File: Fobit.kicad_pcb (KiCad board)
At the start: 2 copper layers, 25.4 x 44.5 mm, 20 parts, among them J1 Conn_01x02, U1 nRF52840, U2 NPM1100-QDAA-R

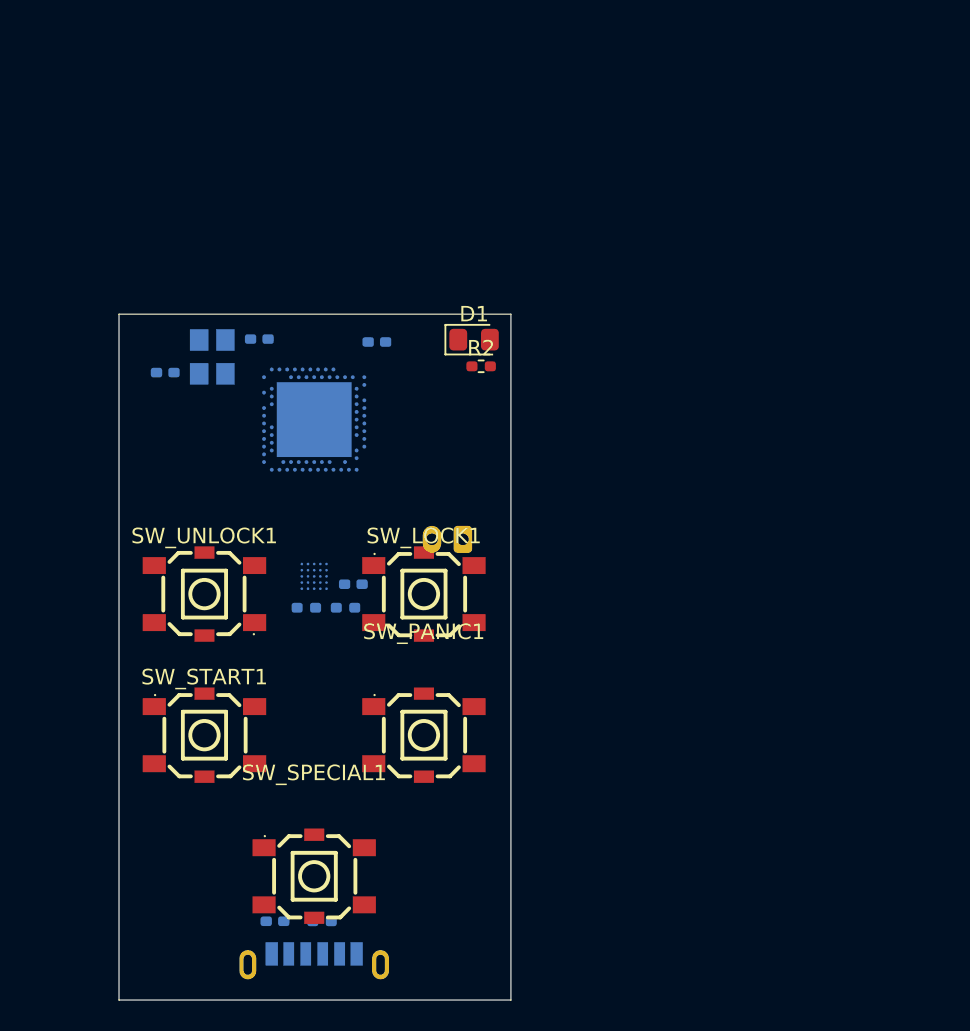
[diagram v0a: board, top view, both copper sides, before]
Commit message: Corrected USB host/slave resistors. Added REG1 DC-DC stage. Removed X2, added X1.
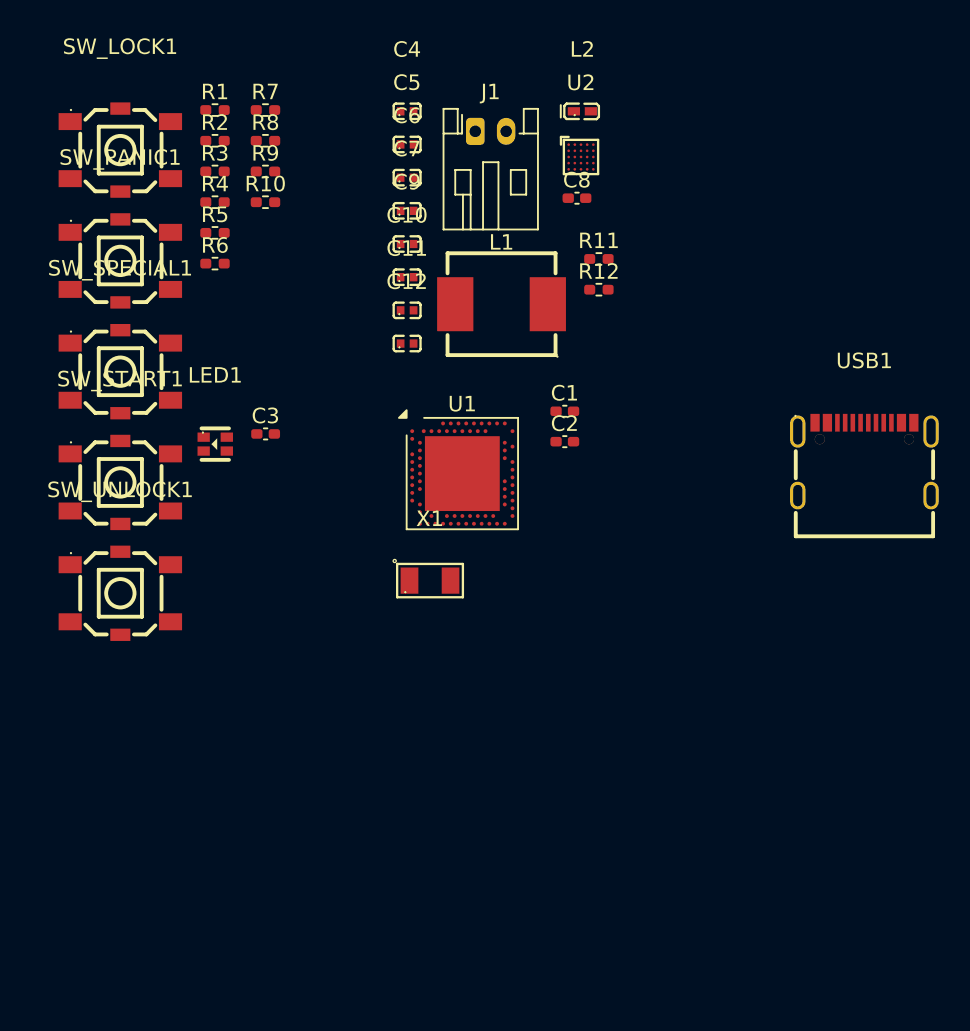
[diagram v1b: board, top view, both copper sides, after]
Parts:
- removed CRYSTAL1: CF4032M00012001, easyeda2kicad:CRYSTAL-SMD_4P-L3.2-W2.5-BL_SIT8008BI
- removed D1: STATUS_LED, LED_SMD:LED_0805_2012Metric_Pad1.15x1.40mm_HandSolder
- added C10: 0402B104K250NT, MyLib:C0402, F.Cu at (158.4, 77.1)
- added C11: TCC0402X5R475M6R3AT, MyLib:C0402, F.Cu at (158.4, 79.3)
- added C12: 0402CG101J500NT, MyLib:C0402, F.Cu at (158.4, 81.4)
- added C4: TCC0402X5R475M6R3AT, MyLib:C0402, F.Cu at (158.4, 66.4)
- added C5: TCC0402X5R475M6R3AT, MyLib:C0402, F.Cu at (158.4, 68.5)
- added C6: CL05A105KA5NQNC, MyLib:C0402, F.Cu at (158.4, 70.7)
- added C9: TCC0402X5R475M6R3AT, MyLib:C0402, F.Cu at (158.4, 75.0)
- added L1: FXL0630-100-M, MyLib:IND-SMD_L7.3-W6.8, F.Cu at (164.5, 78.9)
- added L2: VHF100505HQ15NJT, MyLib:L0402-R-RD, F.Cu at (169.8, 66.4)
- added LED1: SZYY1615RGB-A 4PIN, MyLib:LED-ARRAY-SMD_4P-L1.6-W1.5_SZYY1615RGB-A, F.Cu at (146.0, 87.9)
- added R1: R_Small_US, FobitLib:R_0402_1005Metric_Pad0.72x0.64mm_HandSolder, F.Cu at (146.0, 66.3)
- added R10: R_Small_US, FobitLib:R_0402_1005Metric_Pad0.72x0.64mm_HandSolder, F.Cu at (149.2, 72.3)
- added R11: 4.7kOhms, FobitLib:R_0402_1005Metric_Pad0.72x0.64mm_HandSolder, F.Cu at (170.9, 75.9)
- added R12: 10kOhms, FobitLib:R_0402_1005Metric_Pad0.72x0.64mm_HandSolder, F.Cu at (170.9, 77.9)
- added R3: R_Small_US, FobitLib:R_0402_1005Metric_Pad0.72x0.64mm_HandSolder, F.Cu at (146.0, 70.3)
- added R4: 5.1kOhms, FobitLib:R_0402_1005Metric_Pad0.72x0.64mm_HandSolder, F.Cu at (146.0, 72.3)
- added R5: 5.1kOhms, FobitLib:R_0402_1005Metric_Pad0.72x0.64mm_HandSolder, F.Cu at (146.0, 74.3)
- added R6: R_Small_US, FobitLib:R_0402_1005Metric_Pad0.72x0.64mm_HandSolder, F.Cu at (146.0, 76.2)
- added X1: S3132768092070, MyLib:OSC-SMD_2P-L3.2-W1.5, F.Cu at (159.9, 96.8)
- C1: value 100nF -> 12pF; footprint Capacitor_SMD:C_0402_1005Metric_Pad0.74x0.62mm_HandSolder -> FobitLib:C_0402_1005Metric_Pad0.74x0.62mm_HandSolder; moved to F.Cu
- C2, C8: footprint Capacitor_SMD:C_0402_1005Metric_Pad0.74x0.62mm_HandSolder -> FobitLib:C_0402_1005Metric_Pad0.74x0.62mm_HandSolder; moved to F.Cu
- C3: value 12pF -> 2.2uF; footprint Capacitor_SMD:C_0402_1005Metric_Pad0.74x0.62mm_HandSolder -> FobitLib:C_0402_1005Metric_Pad0.74x0.62mm_HandSolder; moved to F.Cu
- C7: value 2.2uF -> 0402B473K500NT; footprint Capacitor_SMD:C_0402_1005Metric_Pad0.74x0.62mm_HandSolder -> MyLib:C0402; moved to F.Cu
- J1: footprint Connector_JST:JST_PH_S2B-PH-K_1x02_P2.00mm_Horizontal -> FobitLib:JST_PH_S2B-PH-K_1x02_P2.00mm_Horizontal; moved to F.Cu
- R2: value 100Ohms -> R_Small_US; footprint Resistor_SMD:R_0402_1005Metric_Pad0.72x0.64mm_HandSolder -> FobitLib:R_0402_1005Metric_Pad0.72x0.64mm_HandSolder
- R7: value 4.7kOhms -> R_Small_US; footprint Resistor_SMD:R_0402_1005Metric_Pad0.72x0.64mm_HandSolder -> FobitLib:R_0402_1005Metric_Pad0.72x0.64mm_HandSolder; moved to F.Cu
- R8: value 10kOhms -> R_Small_US; footprint Resistor_SMD:R_0402_1005Metric_Pad0.72x0.64mm_HandSolder -> FobitLib:R_0402_1005Metric_Pad0.72x0.64mm_HandSolder; moved to F.Cu
- R9: value 56kOhms -> R_Small_US; footprint Resistor_SMD:R_0402_1005Metric_Pad0.72x0.64mm_HandSolder -> FobitLib:R_0402_1005Metric_Pad0.72x0.64mm_HandSolder; moved to F.Cu
- SW_LOCK1, SW_PANIC1, SW_SPECIAL1, SW_START1, SW_UNLOCK1: footprint easyeda2kicad:SW-SMD_4P-L5.2-W5.2-P3.70-LS6.4_UK-B0233XX -> FobitLib:SW-SMD_4P-L5.2-W5.2-P3.70-LS6.4_UK-B0233XX
- U1: footprint Package_DFN_QFN:Nordic_AQFN-73-1EP_7x7mm_P0.5mm -> FobitLib:Nordic_AQFN-73-1EP_7x7mm_P0.5mm; moved to F.Cu
- U2: footprint easyeda2kicad:WLCSP-25_L2.1-W2.1-R5-C5-P0.40-TL-1 -> FobitLib:WLCSP-25_L2.1-W2.1-R5-C5-P0.40-TL-1; moved to F.Cu
- USB1: value HX TYPE-C 6P LT H5.0 -> TYPE-C16PIN; footprint easyeda2kicad:USB-C-SMD_HX-TYPE-C-6P-LT-H5.0 -> MyLib:USB-C-SMD_TYPE-C16PIN; moved to F.Cu
- moved R9 48.7 mm to (149.2, 70.3), turned to 0 degrees
- moved USB1 48.2 mm to (188.1, 88.9), turned to 0 degrees
- moved C7 46.8 mm to (158.4, 72.8), turned to 0 degrees
- moved SW_PANIC1 36.5 mm to (139.8, 76.1)
- moved SW_SPECIAL1 35.0 mm to (139.8, 83.3)
- moved SW_LOCK1 34.9 mm to (139.8, 68.9)
- moved R7 32.4 mm to (149.2, 66.3)
- moved U2 32.2 mm to (169.7, 69.3), turned to 0 degrees
- moved R8 30.7 mm to (149.2, 68.3)
- moved C8 28.9 mm to (169.4, 72.0)
- moved J1 26.5 mm to (162.8, 67.7), turned to 0 degrees
- moved R2 22.6 mm to (146.0, 68.3)
- moved C2 20.9 mm to (168.6, 87.8)
- moved SW_START1 17.3 mm to (139.8, 90.4)
- moved C1 13.0 mm to (168.6, 85.8)
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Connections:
- C1 pad 1: VBUS -> SOC_XC1
- C3 pad 1: SOC_XC1 -> USBC_V+
- C7 pad 1: USBC_V+ -> SOC_DEC4
- C8 pad 1: VBUS -> SOC_VBUS
- R2 pad 1: STATUS_LED -> LOCK_SIG
- R2 pad 2: Net-(D1-A) -> Net-(R2-Pad2)
- R7 pad 1: BAT_- -> SPECIAL_SIG
- R7 pad 2: Net-(U2-ICHG) -> Net-(R7-Pad2)
- R8 pad 1: Net-(U2-NTC) -> STATUS_LED_R
- R8 pad 2: BAT_- -> Net-(LED1-A-Pad1)
- R9 pad 1: USBC_V+ -> STATUS_LED_G
- R9 pad 2: Net-(USB1-CC1) -> Net-(LED1-A-Pad2)
- SW_LOCK1 pad 1: Net-(R3-Pad2) (its old number) -> Net-(R2-Pad2)
- SW_SPECIAL1 pad 1: Net-(R6-Pad2) (its old number) -> Net-(R7-Pad2)
- U1 pad A22: VBUS -> SOC_VBUS
- U1 pad A23: SOC_XC2 -> unconnected-(U1-XC2-PadA23)
- U1 pad AC17: unconnected-(U1-P0.21-PadAC17) -> UNLOCK_SIG
- U1 pad AC19: unconnected-(U1-P0.23-PadAC19) -> START_SIG
- U1 pad AC21: unconnected-(U1-P0.25-PadAC21) -> SPECIAL_SIG
- U1 pad AC5: unconnected-(U1-DECUSB-PadAC5) -> SOC_DECUSB
- U1 pad AC9: unconnected-(U1-P0.14-PadAC9) -> STATUS_LED_G
- U1 pad AD10: unconnected-(U1-P0.15-PadAD10) -> STATUS_LED_B
- U1 pad AD14: VBUS -> SOC_VBUS
- U1 pad AD18: unconnected-(U1-P0.22-PadAD18) -> LOCK_SIG
- U1 pad AD2: unconnected-(U1-VBUS-PadAD2) -> SOC_VBUS
- U1 pad AD20: unconnected-(U1-P0.24-PadAD20) -> PANIC_SIG
- U1 pad AD23: VBUS -> SOC_VBUS
- U1 pad AD4: unconnected-(U1-D--PadAD4) -> SOC_USB_D-
- U1 pad AD6: unconnected-(U1-D+-PadAD6) -> SOC_USB_D+
- U1 pad AD8: unconnected-(U1-P0.13-PadAD8) -> STATUS_LED_R
- U1 pad B1: VBUS -> SOC_VBUS
- U1 pad B24: SOC_XC1 -> unconnected-(U1-XC1-PadB24)
- U1 pad B3: unconnected-(U1-DCC-PadB3) -> SOC_DCDC_1_DCC
- U1 pad B5: unconnected-(U1-DEC4-PadB5) -> SOC_DEC4
- U1 pad B7: Net-(U1-VSS-PadB7) -> BAT_-
- U1 pad C1: unconnected-(U1-DEC1-PadC1) -> SOC_DEC1
- U1 pad D2: unconnected-(U1-XL1/P0.00-PadD2) -> SOC_XL1
- U1 pad D23: unconnected-(U1-DEC3-PadD23) -> SOC_DEC3
- U1 pad E24: unconnected-(U1-DEC6-PadE24) -> SOC_DEC4
- U1 pad EP: Net-(U1-VSS-PadB7) -> BAT_-
- U1 pad F2: unconnected-(U1-XL2/P0.01-PadF2) -> SOC_XL2
- U1 pad F23: unconnected-(U1-VSS_PA-PadF23) -> BAT_-
- U1 pad W1: VBUS -> SOC_VBUS
- U1 pad Y2: unconnected-(U1-VDDH-PadY2) -> SOC_VBUS
- U2 pad C1: VBUS -> SOC_VBUS
- U2 pad C2: VBUS -> SOC_VBUS
- USB1 pad B5: Net-(USB1-CC1) -> Net-(USB1-CC2)
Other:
- board outline removed
